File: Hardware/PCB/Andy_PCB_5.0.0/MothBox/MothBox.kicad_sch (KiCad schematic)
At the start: 0 parts

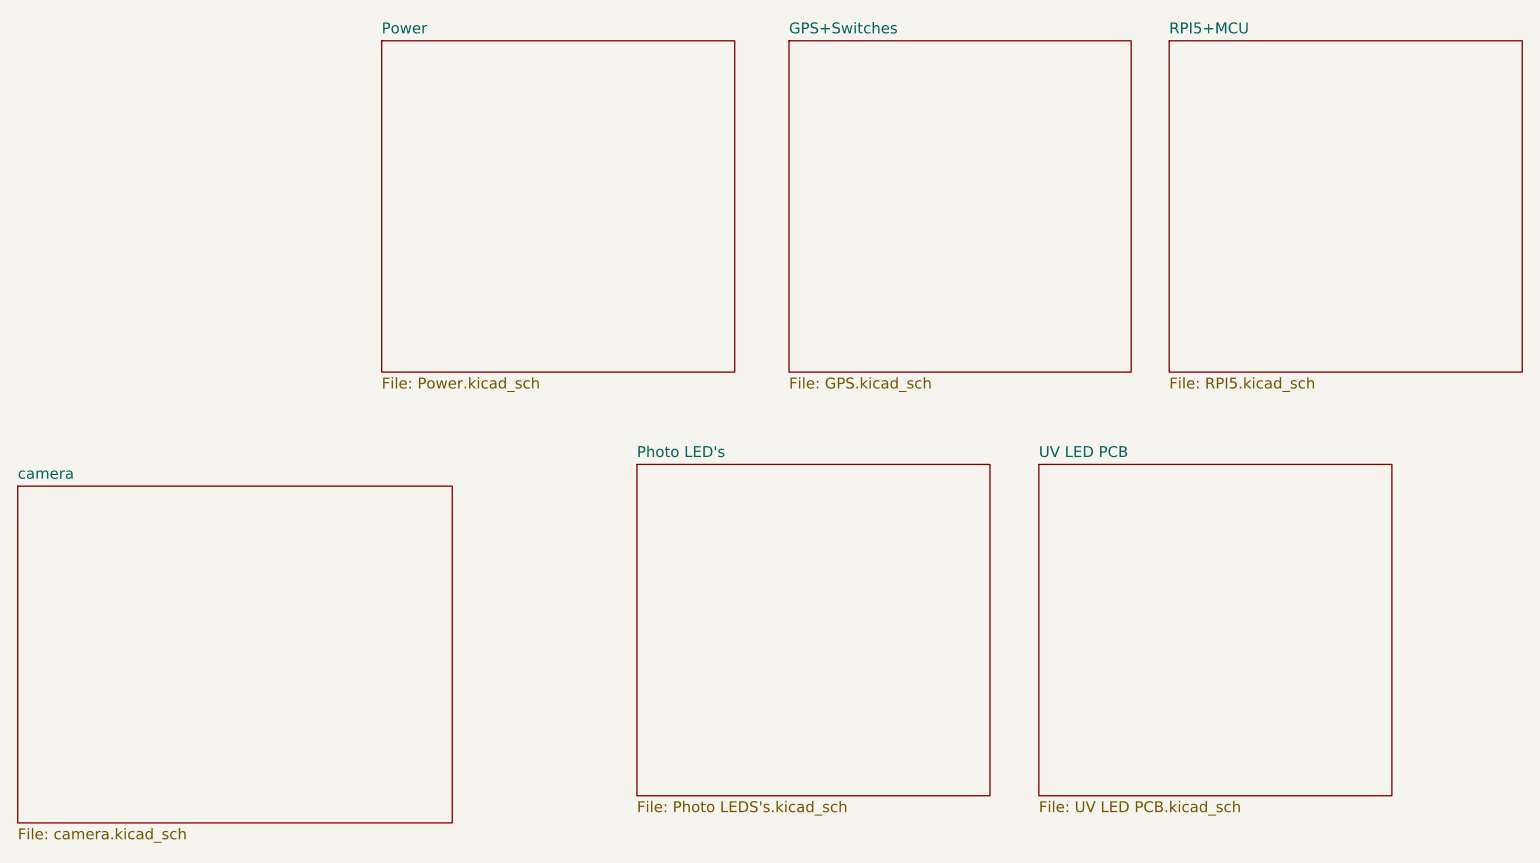
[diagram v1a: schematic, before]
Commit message: added female inverted header
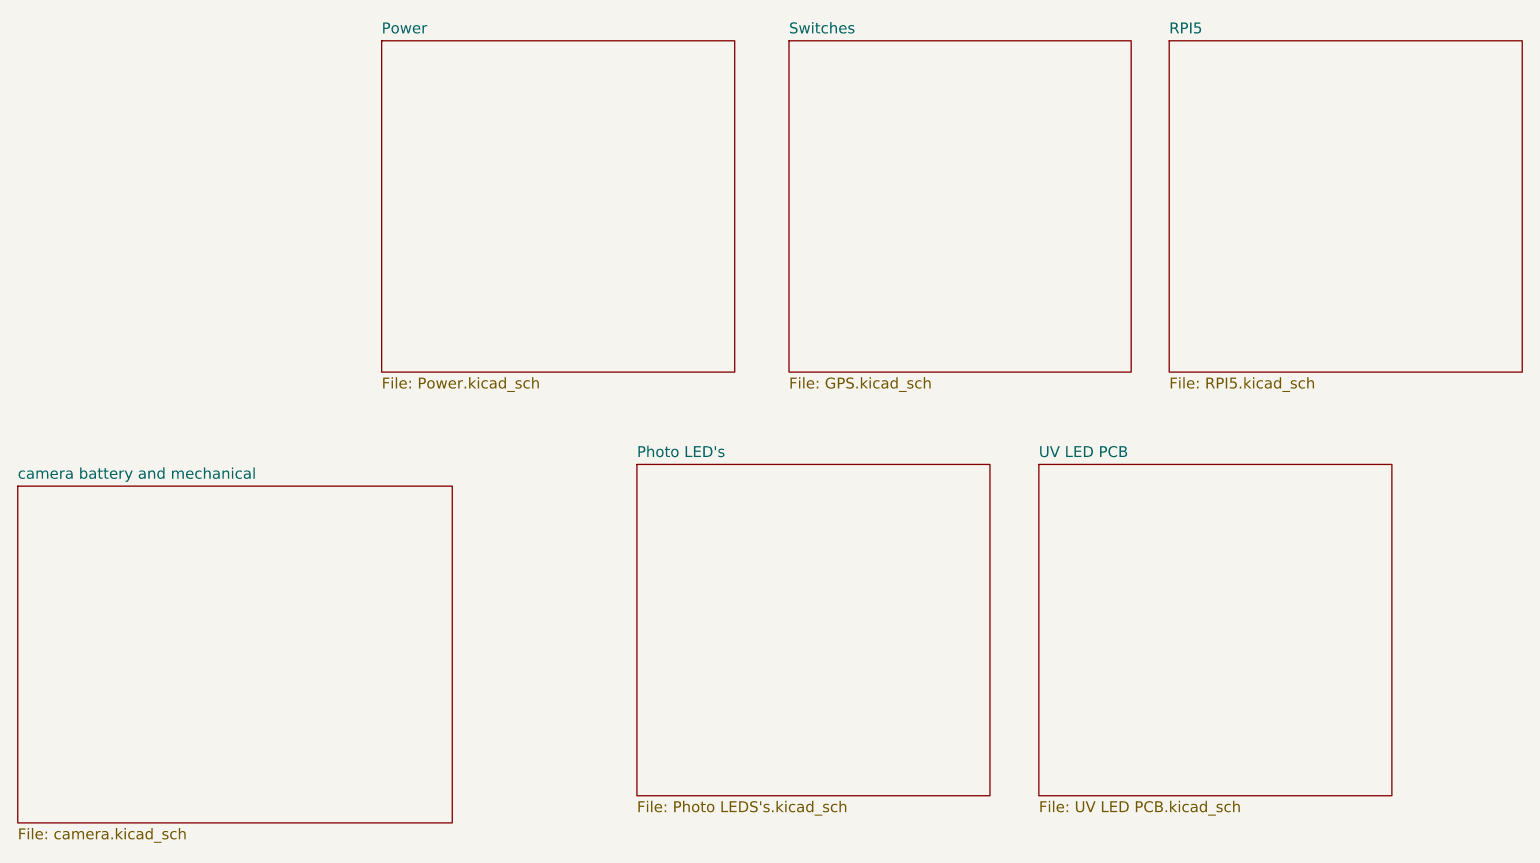
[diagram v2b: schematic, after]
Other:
- sheet GPS+Switches renamed Switches
- sheet RPI5+MCU renamed RPI5
- sheet camera renamed camera battery and mechanical
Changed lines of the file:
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@@
 			(color 0 0 0 0.0000)
 		)
-		(property "Sheetname" "RPI5+MCU"
+		(property "Sheetname" "RPI5"
 			(at 176.53 45.0084 0)
 			(effects
@@
 			(color 0 0 0 0.0000)
 		)
-		(property "Sheetname" "camera"
+		(property "Sheetname" "camera battery and mechanical"
 			(at 41.91 97.0784 0)
 			(effects
@@
 			(color 0 0 0 0.0000)
 		)
-		(property "Sheetname" "GPS+Switches"
+		(property "Sheetname" "Switches"
 			(at 132.08 45.0084 0)
 			(effects

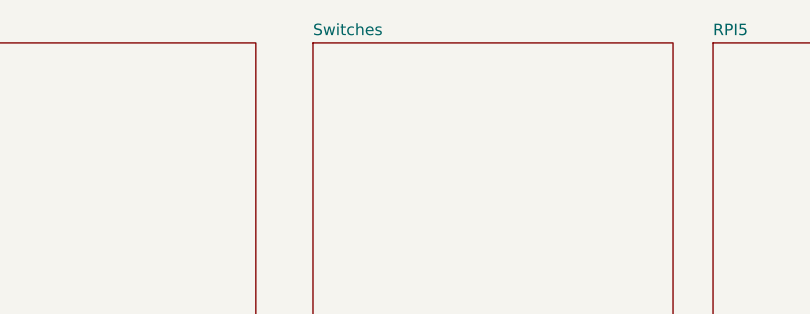
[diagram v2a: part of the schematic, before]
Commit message: Tweaked Mothbeam and added GPS footprints
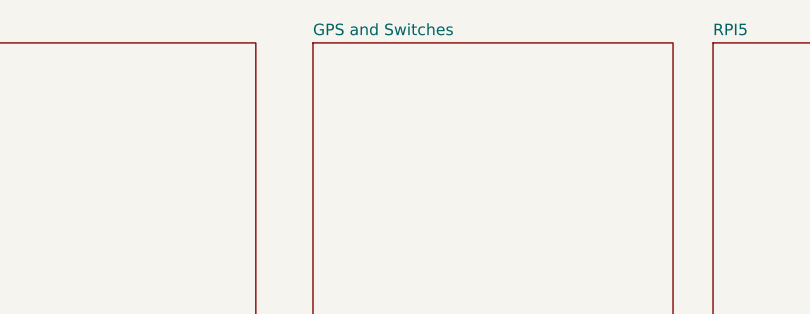
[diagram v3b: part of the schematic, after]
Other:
- sheet Switches renamed GPS and Switches
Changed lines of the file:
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@@
 			(color 0 0 0 0.0000)
 		)
-		(property "Sheetname" "Switches"
+		(property "Sheetname" "GPS and Switches"
 			(at 132.08 45.0084 0)
 			(effects
